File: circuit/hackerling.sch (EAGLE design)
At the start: 42 parts, among them IC1 MCP23017SP, IC2 MCP2300X/P, IC3 MIC5219BM5, SW2 SWITCH_B13EH, U1 MMA8452Q, U2 LCD_16X2, U3 ARDUINOR3-BPLACE, U4 ACCELEROMETER, U5 PCA9306, U6 ACCELEROMETER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

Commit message: removing optional components
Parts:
- removed C5: 10uF, resistor:C-USC0805K
- removed LED3: (no value), SparkFun:LED5MM
- removed R7: (no value), rcl:R-US_R0805
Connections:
- net GND: no longer C5.2
- net IR_OUT1: no longer LED3.C
- net N$19: no longer C5.1, R7.1
- net N$32: no longer LED3.A
- net VCC: no longer R7.2
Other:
- note removed: "Alternate Placing"
- note removed: "SMD"
- note removed: "optional"
- note removed: "replacement"
- moved on the sheet: C4, IR1, R6, U7
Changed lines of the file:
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@@
 <setting verticaltext="up"/>
 </settings>
-<grid distance="0.1" unitdist="inch" unit="inch" style="lines" multiple="1" display="no" altdistance="0.01" altunitdist="inch" altunit="inch"/>
+<grid distance="0.05" unitdist="inch" unit="inch" style="lines" multiple="1" display="no" altdistance="0.01" altunitdist="inch" altunit="inch"/>
 <layers>
 <layer number="1" name="Top" color="4" fill="1" visible="no" active="no"/>
@@
 <part name="C4" library="rcl" deviceset="C-US" device="050-050X075" value="10uF"/>
 <part name="R6" library="resistor" deviceset="R-US_" device="0204/7" value="47"/>
-<part name="R7" library="rcl" deviceset="R-US_" device="R0805"/>
-<part name="C5" library="resistor" deviceset="C-US" device="C0805K" value="10uF"/>
 <part name="JP1" library="SparkFun" deviceset="M02" device="LOCK"/>
 <part name="JP2" library="SparkFun" deviceset="M02" device="LOCK"/>
-<part name="LED3" library="SparkFun" deviceset="LED" device="5MM"/>
 <part name="GND19" library="supply1" deviceset="GND" device=""/>
 <part name="VCC" library="SparkFun" deviceset="5V" device=""/>
@@
 <text x="384.81" y="114.3" size="1.778" layer="91">accelerometer</text>
 <text x="50.8" y="-2.54" size="1.778" layer="91">Check servo pinout</text>
-<wire x1="12.7" y1="100.33" x2="-6.35" y2="100.33" width="0.1524" layer="95" style="shortdash"/>
-<wire x1="-6.35" y1="100.33" x2="-6.35" y2="82.55" width="0.1524" layer="95" style="shortdash"/>
-<wire x1="-6.35" y1="82.55" x2="12.7" y2="82.55" width="0.1524" layer="95" style="shortdash"/>
-<wire x1="12.7" y1="82.55" x2="12.7" y2="100.33" width="0.1524" layer="95" style="shortdash"/>
-<text x="3.81" y="91.44" size="1.778" layer="95">SMD</text>
-<text x="1.27" y="86.36" size="1.778" layer="95">optional</text>
-<text x="-1.27" y="83.82" size="1.778" layer="95">replacement</text>
-<text x="63.5" y="144.78" size="1.778" layer="95" rot="R180">Alternate Placing</text>
-<wire x1="40.64" y1="128.27" x2="66.04" y2="128.27" width="0.1524" layer="95"/>
-<wire x1="66.04" y1="128.27" x2="66.04" y2="148.59" width="0.1524" layer="95"/>
-<wire x1="66.04" y1="148.59" x2="40.64" y2="148.59" width="0.1524" layer="95"/>
-<wire x1="40.64" y1="148.59" x2="40.64" y2="128.27" width="0.1524" layer="95"/>
 <text x="-187.96" y="68.58" size="1.778" layer="95">Unconnected</text>
 <text x="-184.15" y="64.77" size="1.778" layer="95">Btn1</text>
@@
 <instance part="P+6" gate="VCC" x="129.54" y="71.12"/>
 <instance part="P+7" gate="VCC" x="190.5" y="86.36"/>
-<instance part="IR1" gate="G$1" x="-38.1" y="109.22"/>
-<instance part="GND9" gate="1" x="-20.32" y="82.55"/>
-<instance part="P+8" gate="VCC" x="10.16" y="106.68"/>
+<instance part="IR1" gate="G$1" x="-38.1" y="109.22" rot="MR180"/>
+<instance part="GND9" gate="1" x="-12.7" y="106.68"/>
+<instance part="P+8" gate="VCC" x="-5.08" y="139.7"/>
 <instance part="U4" gate="G$1" x="-20.32" y="25.4" rot="MR0"/>
 <instance part="GND10" gate="1" x="-35.56" y="22.86" rot="MR0"/>
@@
 <instance part="P+15" gate="G$1" x="426.72" y="58.42"/>
 <instance part="U6" gate="G$1" x="-40.64" y="-12.7" rot="MR0"/>
-<instance part="U7" gate="G$1" x="50.8" y="86.36"/>
+<instance part="U7" gate="G$1" x="60.96" y="86.36"/>
 <instance part="P+16" gate="VCC" x="-22.86" y="2.54"/>
 <instance part="GND17" gate="1" x="-50.8" y="-17.78" rot="MR0"/>
@@
 <instance part="U8" gate="G$1" x="180.34" y="68.58" rot="MR180"/>
 <instance part="P+17" gate="VCC" x="185.42" y="25.4"/>
-<instance part="C4" gate="G$1" x="-16.51" y="101.6"/>
-<instance part="R6" gate="G$1" x="0" y="104.14"/>
-<instance part="R7" gate="G$1" x="5.08" y="96.52"/>
-<instance part="C5" gate="G$1" x="-2.54" y="91.44"/>
+<instance part="C4" gate="G$1" x="-5.08" y="114.3"/>
+<instance part="R6" gate="G$1" x="-5.08" y="128.27" rot="R90"/>
 <instance part="JP1" gate="G$1" x="116.84" y="53.34" rot="R180"/>
 <instance part="JP2" gate="G$1" x="116.84" y="39.37" rot="R180"/>
-<instance part="LED3" gate="G$1" x="57.15" y="137.16"/>
 <instance part="GND19" gate="1" x="-91.44" y="-3.81" rot="MR0"/>
 <instance part="VCC" gate="G$1" x="365.76" y="101.6"/>
@@
 <wire x1="60.96" y1="76.2" x2="60.96" y2="78.74" width="0.1524" layer="91"/>
 <pinref part="U7" gate="G$1" pin="A"/>
-<wire x1="60.96" y1="78.74" x2="50.8" y2="78.74" width="0.1524" layer="91"/>
 </segment>
 <segment>
@@
 <pinref part="GND9" gate="1" pin="GND"/>
 <pinref part="IR1" gate="G$1" pin="GND"/>
-<wire x1="-20.32" y1="86.36" x2="-20.32" y2="93.98" width="0.1524" layer="91"/>
-<wire x1="-20.32" y1="93.98" x2="-20.32" y2="109.22" width="0.1524" layer="91"/>
-<wire x1="-20.32" y1="109.22" x2="-27.94" y2="109.22" width="0.1524" layer="91"/>
+<wire x1="-12.7" y1="109.22" x2="-27.94" y2="109.22" width="0.1524" layer="91"/>
 <pinref part="C4" gate="G$1" pin="2"/>
-<wire x1="-16.51" y1="96.52" x2="-16.51" y2="93.98" width="0.1524" layer="91"/>
-<wire x1="-16.51" y1="93.98" x2="-20.32" y2="93.98" width="0.1524" layer="91"/>
-<junction x="-20.32" y="93.98"/>
-<wire x1="-20.32" y1="85.09" x2="-20.32" y2="86.36" width="0.1524" layer="91"/>
-<wire x1="-20.32" y1="86.36" x2="-2.54" y2="86.36" width="0.1524" layer="91"/>
-<junction x="-20.32" y="85.09"/>
-<pinref part="C5" gate="G$1" pin="2"/>
+<junction x="-12.7" y="109.22"/>
+<wire x1="-5.08" y1="109.22" x2="-12.7" y2="109.22" width="0.1524" layer="91"/>
 </segment>
 <segment>
@@
 <wire x1="60.96" y1="93.98" x2="60.96" y2="96.52" width="0.1524" layer="91"/>
 <pinref part="U7" gate="G$1" pin="E"/>
-<wire x1="60.96" y1="93.98" x2="50.8" y2="93.98" width="0.1524" layer="91"/>
 </segment>
 <segment>
@@
 <pinref part="P+8" gate="VCC" pin="VCC"/>
 <pinref part="R6" gate="G$1" pin="2"/>
-<wire x1="5.08" y1="104.14" x2="10.16" y2="104.14" width="0.1524" layer="91"/>
-<pinref part="R7" gate="G$1" pin="2"/>
-<wire x1="10.16" y1="96.52" x2="10.16" y2="104.14" width="0.1524" layer="91"/>
-<junction x="10.16" y="104.14"/>
+<wire x1="-5.08" y1="133.35" x2="-5.08" y2="137.16" width="0.1524" layer="91"/>
 </segment>
 <segment>
@@
 <net name="POT" class="0">
 <segment>
-<wire x1="66.04" y1="86.36" x2="73.66" y2="86.36" width="0.1524" layer="91"/>
 <label x="68.58" y="86.36" size="1.778" layer="95"/>
 <pinref part="U7" gate="G$1" pin="S"/>
-<wire x1="55.88" y1="86.36" x2="58.42" y2="86.36" width="0.1524" layer="91"/>
-<wire x1="58.42" y1="86.36" x2="58.42" y2="91.44" width="0.1524" layer="91"/>
-<wire x1="58.42" y1="91.44" x2="66.04" y2="91.44" width="0.1524" layer="91"/>
-<wire x1="66.04" y1="91.44" x2="66.04" y2="86.36" width="0.1524" layer="91"/>
+<wire x1="66.04" y1="86.36" x2="73.66" y2="86.36" width="0.1524" layer="91"/>
 </segment>
 <segment>
@@
 <segment>
 <pinref part="IR1" gate="G$1" pin="OUT"/>
-<wire x1="-27.94" y1="114.3" x2="-15.24" y2="114.3" width="0.1524" layer="91"/>
-<label x="-25.4" y="114.3" size="1.778" layer="95"/>
+<wire x1="-27.94" y1="104.14" x2="-19.05" y2="104.14" width="0.1524" layer="91"/>
+<label x="-24.13" y="104.14" size="1.778" layer="95"/>
 </segment>
 <segment>
@@
 <wire x1="73.66" y1="109.22" x2="83.82" y2="109.22" width="0.1524" layer="91"/>
 <wire x1="57.15" y1="130.81" x2="69.85" y2="130.81" width="0.1524" layer="91"/>
-<pinref part="LED3" gate="G$1" pin="C"/>
 <wire x1="57.15" y1="130.81" x2="57.15" y2="132.08" width="0.1524" layer="91"/>
 <label x="59.69" y="130.81" size="1.778" layer="95"/>
@@
 <net name="N$19" class="0">
 <segment>
-<pinref part="C5" gate="G$1" pin="1"/>
-<pinref part="R7" gate="G$1" pin="1"/>
-<wire x1="0" y1="96.52" x2="-2.54" y2="93.98" width="0.1524" layer="91"/>
 <pinref part="IR1" gate="G$1" pin="VCC"/>
 <pinref part="C4" gate="G$1" pin="1"/>
-<wire x1="-5.08" y1="104.14" x2="-27.94" y2="104.14" width="0.1524" layer="91"/>
 <pinref part="R6" gate="G$1" pin="1"/>
-<junction x="-5.08" y="104.14"/>
-<wire x1="-5.08" y1="104.14" x2="-16.51" y2="104.14" width="0.1524" layer="91"/>
-<wire x1="-2.54" y1="93.98" x2="-5.08" y2="93.98" width="0.1524" layer="91"/>
-<wire x1="-5.08" y1="93.98" x2="-5.08" y2="104.14" width="0.1524" layer="91"/>
-<junction x="-2.54" y="93.98"/>
+<junction x="-5.08" y="123.19"/>
+<wire x1="-5.08" y1="116.84" x2="-13.97" y2="116.84" width="0.1524" layer="91"/>
+<wire x1="-13.97" y1="116.84" x2="-13.97" y2="114.3" width="0.1524" layer="91"/>
+<wire x1="-13.97" y1="114.3" x2="-27.94" y2="114.3" width="0.1524" layer="91"/>
+<wire x1="-5.08" y1="123.19" x2="-5.08" y2="116.84" width="0.1524" layer="91"/>
 </segment>
 </net>
@@
 <net name="N$32" class="0">
 <segment>
-<pinref part="LED3" gate="G$1" pin="A"/>
 <wire x1="57.15" y1="139.7" x2="57.15" y2="140.97" width="0.1524" layer="91"/>
 <wire x1="57.15" y1="140.97" x2="96.52" y2="140.97" width="0.1524" layer="91"/>

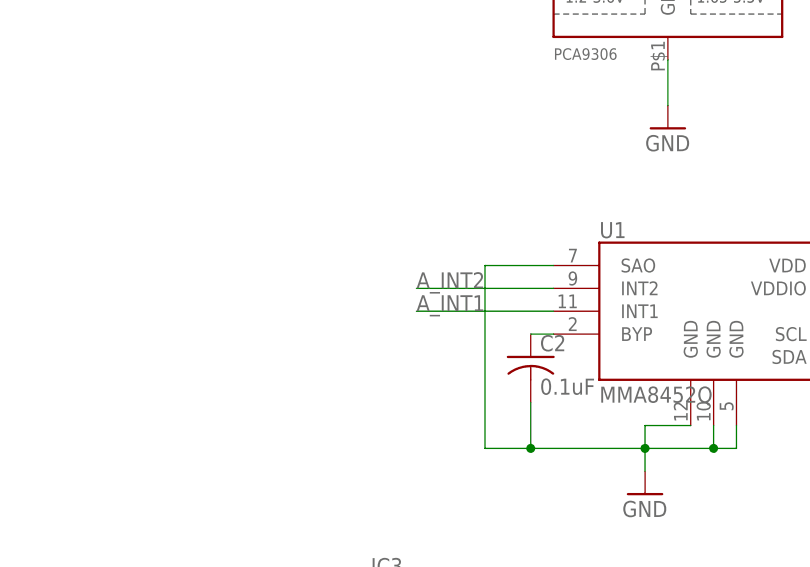
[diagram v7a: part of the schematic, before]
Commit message: adding resistors to interrupt
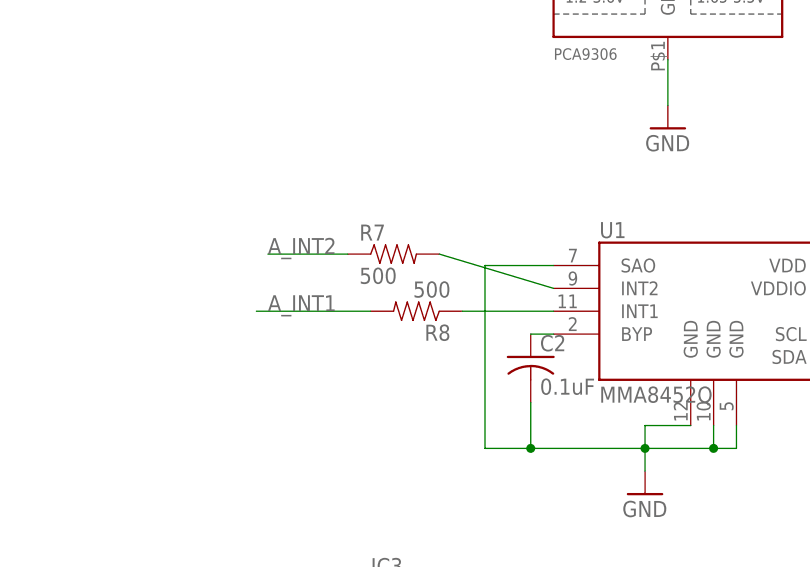
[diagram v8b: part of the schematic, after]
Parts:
- added R7, R8: 500, SparkFun:RESISTOR0603-RES
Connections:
- new net N$6: R7.2, U1.INT2
- new net N$7: R8.1, U1.INT1
- net A_INT1: now also R8.2; no longer U1.INT1
- net A_INT2: now also R7.1; no longer U1.INT2
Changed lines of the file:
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@@
 <part name="GND19" library="supply1" deviceset="GND" device=""/>
 <part name="VCC" library="SparkFun" deviceset="5V" device=""/>
+<part name="R7" library="SparkFun" deviceset="RESISTOR" device="0603-RES" value="500"/>
+<part name="R8" library="SparkFun" deviceset="RESISTOR" device="0603-RES" value="500"/>
 </parts>
 <sheets>
@@
 <instance part="GND19" gate="1" x="-91.44" y="-3.81" rot="MR0"/>
 <instance part="VCC" gate="G$1" x="365.76" y="101.6"/>
+<instance part="R7" gate="G$1" x="365.76" y="46.99"/>
+<instance part="R8" gate="G$1" x="368.3" y="40.64" rot="R180"/>
 </instances>
 <busses>
@@
 </segment>
 <segment>
-<pinref part="U1" gate="G$1" pin="INT2"/>
-<wire x1="383.54" y1="43.18" x2="368.3" y2="43.18" width="0.1524" layer="91"/>
-<label x="368.3" y="43.18" size="1.778" layer="95"/>
+<wire x1="360.68" y1="46.99" x2="351.79" y2="46.99" width="0.1524" layer="91"/>
+<label x="351.79" y="46.99" size="1.778" layer="95"/>
+<pinref part="R7" gate="G$1" pin="1"/>
 </segment>
 </net>
@@
 </segment>
 <segment>
-<pinref part="U1" gate="G$1" pin="INT1"/>
-<wire x1="383.54" y1="40.64" x2="368.3" y2="40.64" width="0.1524" layer="91"/>
-<label x="368.3" y="40.64" size="1.778" layer="95"/>
+<wire x1="363.22" y1="40.64" x2="350.52" y2="40.64" width="0.1524" layer="91"/>
+<label x="351.79" y="40.64" size="1.778" layer="95"/>
+<pinref part="R8" gate="G$1" pin="2"/>
 </segment>
 </net>
@@
 </segment>
 </net>
+<net name="N$6" class="0">
+<segment>
+<pinref part="R7" gate="G$1" pin="2"/>
+<pinref part="U1" gate="G$1" pin="INT2"/>
+<wire x1="370.84" y1="46.99" x2="383.54" y2="43.18" width="0.1524" layer="91"/>
+</segment>
+</net>
+<net name="N$7" class="0">
+<segment>
+<pinref part="U1" gate="G$1" pin="INT1"/>
+<pinref part="R8" gate="G$1" pin="1"/>
+<wire x1="373.38" y1="40.64" x2="383.54" y2="40.64" width="0.1524" layer="91"/>
+</segment>
+</net>
